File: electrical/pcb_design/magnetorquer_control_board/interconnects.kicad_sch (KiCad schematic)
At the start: 7 parts, among them J2 Molex_504050-1291, J3 Molex_504050-1291, J4 Molex_504050-0891, J5 Molex_504050-0891, J6 Molex_504050-0491, J7 STLINK, J8 STLINK

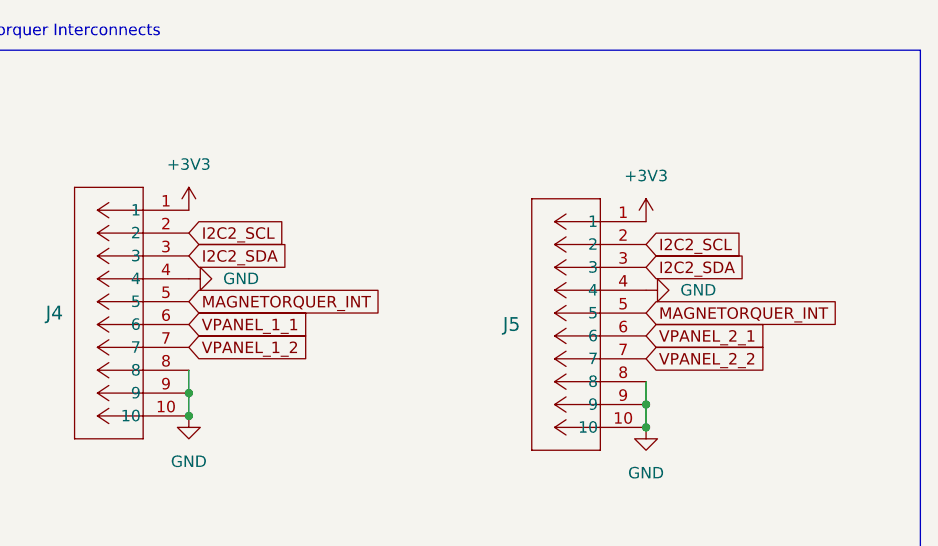
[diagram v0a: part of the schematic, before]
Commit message: Fix order of signals in connectors to magnetorquers.
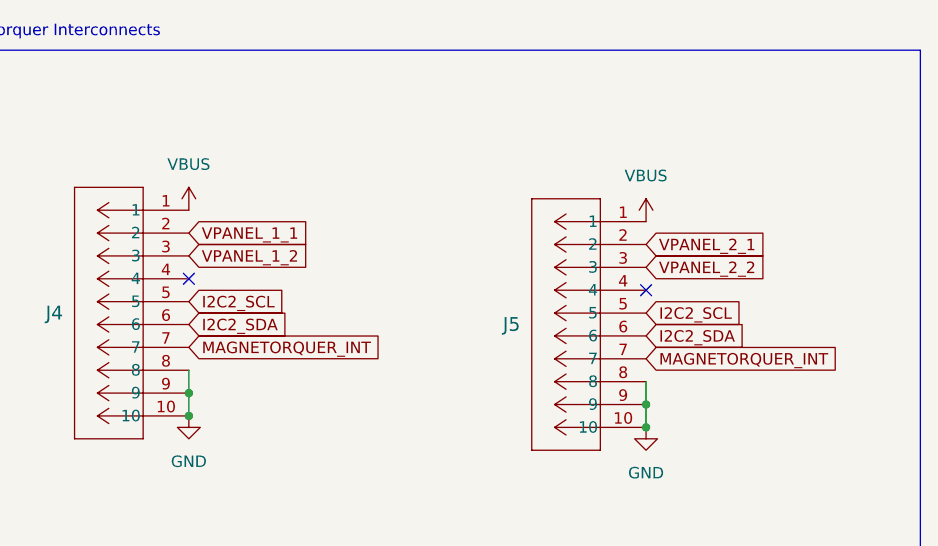
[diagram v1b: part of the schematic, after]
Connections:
- net +3V3: no longer J4.1, J5.1
- net GND: no longer J4.4, J5.4
- net I2C2_SCL: now also J4.5, J5.5; no longer J4.2, J5.2
- net I2C2_SDA: now also J4.6, J5.6; no longer J4.3, J5.3
- net MAGNETORQUER_INT: now also J4.7, J5.7; no longer J4.5, J5.5
- net VBUS: now also J4.1, J5.1
- net VPANEL_1_1: now also J4.2; no longer J4.6
- net VPANEL_1_2: now also J4.3; no longer J4.7
- net VPANEL_2_1: now also J5.2; no longer J5.6
- net VPANEL_2_2: now also J5.3; no longer J5.7
- no-connect marks 6 -> 8
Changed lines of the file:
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@@
   (junction (at 248.92 60.96) (diameter 0) (color 0 0 0 0)
   )
+  (no_connect (at 198.12 44.45))
   (no_connect (at 54.61 64.77))
   (no_connect (at 93.98 64.77))
   (no_connect (at 54.61 54.61))
   (no_connect (at 54.61 57.15))
+  (no_connect (at 248.92 45.72))
   (no_connect (at 93.98 57.15))
   (no_connect (at 93.98 54.61))
@@
     (effects (font (size 1.27 1.27)) (justify left bottom))
   )
-  (global_label "I2C2_SDA" (shape input) (at 248.92 43.18 0) (fields_autoplaced)
-    (effects (font (size 1.27 1.27)) (justify left))
-    (property "Intersheetrefs" "${INTERSHEET_REFS}" (at 260.7347 43.18 0)
+  (global_label "MAGNETORQUER_INT" (shape input) (at 198.12 52.07 0) (fields_autoplaced)
+    (effects (font (size 1.27 1.27)) (justify left))
+    (property "Intersheetrefs" "${INTERSHEET_REFS}" (at 219.9133 52.07 0)
       (effects (font (size 1.27 1.27)) (justify left) hide)
     )
@@
     )
   )
+  (global_label "VPANEL_1_2" (shape input) (at 198.12 41.91 0) (fields_autoplaced)
+    (effects (font (size 1.27 1.27)) (justify left))
+    (property "Intersheetrefs" "${INTERSHEET_REFS}" (at 212.4142 41.91 0)
+      (effects (font (size 1.27 1.27)) (justify left) hide)
+    )
+  )
   (global_label "NRST" (shape input) (at 93.98 44.45 180) (fields_autoplaced)
     (effects (font (size 1.27 1.27)) (justify right))
@@
     )
   )
+  (global_label "MAGNETORQUER_INT" (shape input) (at 248.92 53.34 0) (fields_autoplaced)
+    (effects (font (size 1.27 1.27)) (justify left))
+    (property "Intersheetrefs" "${INTERSHEET_REFS}" (at 270.7133 53.34 0)
+      (effects (font (size 1.27 1.27)) (justify left) hide)
+    )
+  )
   (global_label "TRACESWO" (shape input) (at 236.22 133.35 180) (fields_autoplaced)
     (effects (font (size 1.27 1.27)) (justify right))
@@
     )
   )
-  (global_label "VPANEL_1_2" (shape input) (at 198.12 52.07 0) (fields_autoplaced)
-    (effects (font (size 1.27 1.27)) (justify left))
-    (property "Intersheetrefs" "${INTERSHEET_REFS}" (at 212.4142 52.07 0)
-      (effects (font (size 1.27 1.27)) (justify left) hide)
-    )
-  )
-  (global_label "I2C2_SCL" (shape input) (at 248.92 40.64 0) (fields_autoplaced)
-    (effects (font (size 1.27 1.27)) (justify left))
-    (property "Intersheetrefs" "${INTERSHEET_REFS}" (at 260.6742 40.64 0)
-      (effects (font (size 1.27 1.27)) (justify left) hide)
-    )
-  )
-  (global_label "I2C2_SCL" (shape input) (at 198.12 39.37 0) (fields_autoplaced)
-    (effects (font (size 1.27 1.27)) (justify left))
-    (property "Intersheetrefs" "${INTERSHEET_REFS}" (at 209.8742 39.37 0)
-      (effects (font (size 1.27 1.27)) (justify left) hide)
-    )
-  )
-  (global_label "I2C2_SDA" (shape input) (at 198.12 41.91 0) (fields_autoplaced)
-    (effects (font (size 1.27 1.27)) (justify left))
-    (property "Intersheetrefs" "${INTERSHEET_REFS}" (at 209.9347 41.91 0)
+  (global_label "I2C2_SDA" (shape input) (at 248.92 50.8 0) (fields_autoplaced)
+    (effects (font (size 1.27 1.27)) (justify left))
+    (property "Intersheetrefs" "${INTERSHEET_REFS}" (at 260.7347 50.8 0)
       (effects (font (size 1.27 1.27)) (justify left) hide)
     )
@@
     )
   )
+  (global_label "I2C2_SCL" (shape input) (at 198.12 46.99 0) (fields_autoplaced)
+    (effects (font (size 1.27 1.27)) (justify left))
+    (property "Intersheetrefs" "${INTERSHEET_REFS}" (at 209.8742 46.99 0)
+      (effects (font (size 1.27 1.27)) (justify left) hide)
+    )
+  )
   (global_label "CANL" (shape input) (at 93.98 62.23 180) (fields_autoplaced)
     (effects (font (size 1.27 1.27)) (justify right))
@@
     )
   )
-  (global_label "VPANEL_1_1" (shape input) (at 198.12 49.53 0) (fields_autoplaced)
-    (effects (font (size 1.27 1.27)) (justify left))
-    (property "Intersheetrefs" "${INTERSHEET_REFS}" (at 212.4142 49.53 0)
-      (effects (font (size 1.27 1.27)) (justify left) hide)
-    )
-  )
-  (global_label "VPANEL_2_1" (shape input) (at 248.92 50.8 0) (fields_autoplaced)
-    (effects (font (size 1.27 1.27)) (justify left))
-    (property "Intersheetrefs" "${INTERSHEET_REFS}" (at 263.2142 50.8 0)
-      (effects (font (size 1.27 1.27)) (justify left) hide)
-    )
-  )
   (global_label "SWDIO" (shape input) (at 93.98 41.91 180) (fields_autoplaced)
     (effects (font (size 1.27 1.27)) (justify right))
@@
     )
   )
-  (global_label "MAGNETORQUER_INT" (shape input) (at 198.12 46.99 0) (fields_autoplaced)
-    (effects (font (size 1.27 1.27)) (justify left))
-    (property "Intersheetrefs" "${INTERSHEET_REFS}" (at 219.9133 46.99 0)
-      (effects (font (size 1.27 1.27)) (justify left) hide)
-    )
-  )
-  (global_label "MAGNETORQUER_INT" (shape input) (at 248.92 48.26 0) (fields_autoplaced)
-    (effects (font (size 1.27 1.27)) (justify left))
-    (property "Intersheetrefs" "${INTERSHEET_REFS}" (at 270.7133 48.26 0)
+  (global_label "I2C2_SDA" (shape input) (at 198.12 49.53 0) (fields_autoplaced)
+    (effects (font (size 1.27 1.27)) (justify left))
+    (property "Intersheetrefs" "${INTERSHEET_REFS}" (at 209.9347 49.53 0)
+      (effects (font (size 1.27 1.27)) (justify left) hide)
+    )
+  )
+  (global_label "I2C2_SCL" (shape input) (at 248.92 48.26 0) (fields_autoplaced)
+    (effects (font (size 1.27 1.27)) (justify left))
+    (property "Intersheetrefs" "${INTERSHEET_REFS}" (at 260.6742 48.26 0)
       (effects (font (size 1.27 1.27)) (justify left) hide)
     )
@@
     )
   )
-  (global_label "VPANEL_2_2" (shape input) (at 248.92 53.34 0) (fields_autoplaced)
-    (effects (font (size 1.27 1.27)) (justify left))
-    (property "Intersheetrefs" "${INTERSHEET_REFS}" (at 263.2142 53.34 0)
+  (global_label "VPANEL_2_1" (shape input) (at 248.92 40.64 0) (fields_autoplaced)
+    (effects (font (size 1.27 1.27)) (justify left))
+    (property "Intersheetrefs" "${INTERSHEET_REFS}" (at 263.2142 40.64 0)
       (effects (font (size 1.27 1.27)) (justify left) hide)
     )
@@
     )
   )
+  (global_label "VPANEL_1_1" (shape input) (at 198.12 39.37 0) (fields_autoplaced)
+    (effects (font (size 1.27 1.27)) (justify left))
+    (property "Intersheetrefs" "${INTERSHEET_REFS}" (at 212.4142 39.37 0)
+      (effects (font (size 1.27 1.27)) (justify left) hide)
+    )
+  )
   (global_label "TRACESWO" (shape input) (at 203.2 133.35 180) (fields_autoplaced)
     (effects (font (size 1.27 1.27)) (justify right))
@@
     (property "Intersheetrefs" "${INTERSHEET_REFS}" (at 46.6658 132.08 0)
       (effects (font (size 1.27 1.27)) (justify right) hide)
+    )
+  )
+  (global_label "VPANEL_2_2" (shape input) (at 248.92 43.18 0) (fields_autoplaced)
+    (effects (font (size 1.27 1.27)) (justify left))
+    (property "Intersheetrefs" "${INTERSHEET_REFS}" (at 263.2142 43.18 0)
+      (effects (font (size 1.27 1.27)) (justify left) hide)
     )
   )
@@
     )
   )
-  (symbol (lib_id "power:GND") (at 248.92 45.72 90) (unit 1)
-    (in_bom yes) (on_board yes) (dnp no) (fields_autoplaced)
-    (property "Reference" "#PWR069" (at 255.27 45.72 0)
-      (effects (font (size 1.27 1.27)) hide)
-    )
-    (property "Value" "GND" (at 252.73 45.72 90)
-      (effects (font (size 1.27 1.27)) (justify right))
-    )
-    (property "Footprint" "" (at 248.92 45.72 0)
-      (effects (font (size 1.27 1.27)) hide)
-    )
-    (property "Datasheet" "" (at 248.92 45.72 0)
-      (effects (font (size 1.27 1.27)) hide)
-    )
-    (pin "1")
-    (instances
-      (project "magnetorquer_control_board"
-        (path "/695f882b-5312-4493-b26d-8f7d6768a9db/26d39f3e-c102-47df-b5c8-40df03104ca4"
-          (reference "#PWR069") (unit 1)
-        )
-      )
-    )
-  )
-  (symbol (lib_id "power:+3V3") (at 248.92 38.1 0) (mirror y) (unit 1)
-    (in_bom yes) (on_board yes) (dnp no)
-    (property "Reference" "#PWR067" (at 248.92 41.91 0)
-      (effects (font (size 1.27 1.27)) hide)
-    )
-    (property "Value" "+3V3" (at 248.92 33.02 0)
+  (symbol (lib_id "power:VBUS") (at 248.92 38.1 0) (unit 1)
+    (in_bom yes) (on_board yes) (dnp no) (fields_autoplaced)
+    (property "Reference" "#PWR075" (at 248.92 41.91 0)
+      (effects (font (size 1.27 1.27)) hide)
+    )
+    (property "Value" "VBUS" (at 248.92 33.02 0)
       (effects (font (size 1.27 1.27)))
     )
@@
       (project "magnetorquer_control_board"
         (path "/695f882b-5312-4493-b26d-8f7d6768a9db/26d39f3e-c102-47df-b5c8-40df03104ca4"
-          (reference "#PWR067") (unit 1)
+          (reference "#PWR075") (unit 1)
         )
       )
@@
         (path "/695f882b-5312-4493-b26d-8f7d6768a9db/26d39f3e-c102-47df-b5c8-40df03104ca4"
           (reference "#PWR061") (unit 1)
-        )
-      )
-    )
-  )
-  (symbol (lib_id "power:GND") (at 198.12 44.45 90) (unit 1)
-    (in_bom yes) (on_board yes) (dnp no) (fields_autoplaced)
-    (property "Reference" "#PWR065" (at 204.47 44.45 0)
-      (effects (font (size 1.27 1.27)) hide)
-    )
-    (property "Value" "GND" (at 201.93 44.45 90)
-      (effects (font (size 1.27 1.27)) (justify right))
-    )
-    (property "Footprint" "" (at 198.12 44.45 0)
-      (effects (font (size 1.27 1.27)) hide)
-    )
-    (property "Datasheet" "" (at 198.12 44.45 0)
-      (effects (font (size 1.27 1.27)) hide)
-    )
-    (pin "1")
-    (instances
-      (project "magnetorquer_control_board"
-        (path "/695f882b-5312-4493-b26d-8f7d6768a9db/26d39f3e-c102-47df-b5c8-40df03104ca4"
-          (reference "#PWR065") (unit 1)
         )
       )
@@
     )
   )
-  (symbol (lib_id "power:+3V3") (at 198.12 36.83 0) (mirror y) (unit 1)
-    (in_bom yes) (on_board yes) (dnp no)
+  (symbol (lib_id "power:VBUS") (at 198.12 36.83 0) (unit 1)
+    (in_bom yes) (on_board yes) (dnp no) (fields_autoplaced)
     (property "Reference" "#PWR064" (at 198.12 40.64 0)
       (effects (font (size 1.27 1.27)) hide)
     )
-    (property "Value" "+3V3" (at 198.12 31.75 0)
-      (effects (font (size 1.27 1.27)))
-    )
+    (property "Value" "VBUS" (at 198.12 31.75 0)
+      (effects (font (size 1.27 1.27)))
+    )
